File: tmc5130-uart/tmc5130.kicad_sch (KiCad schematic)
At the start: 30 parts, among them J401 Molex_Pico-SPOX_Horizontal, J402 Molex_Pico-Clasp_Horizontal, U401 TMC5160A-WA, U402 MAX6816, X401 16MHz

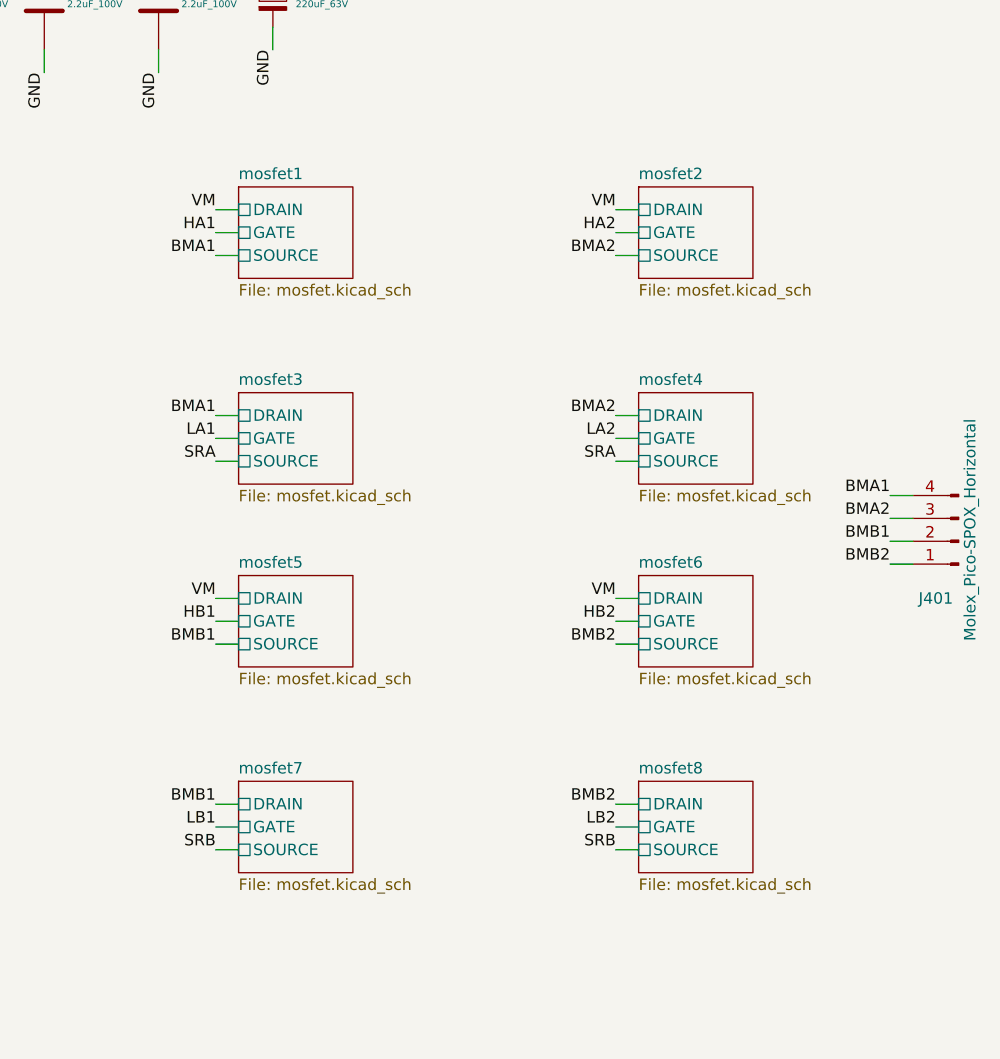
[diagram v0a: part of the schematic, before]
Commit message: Delete unused schematics
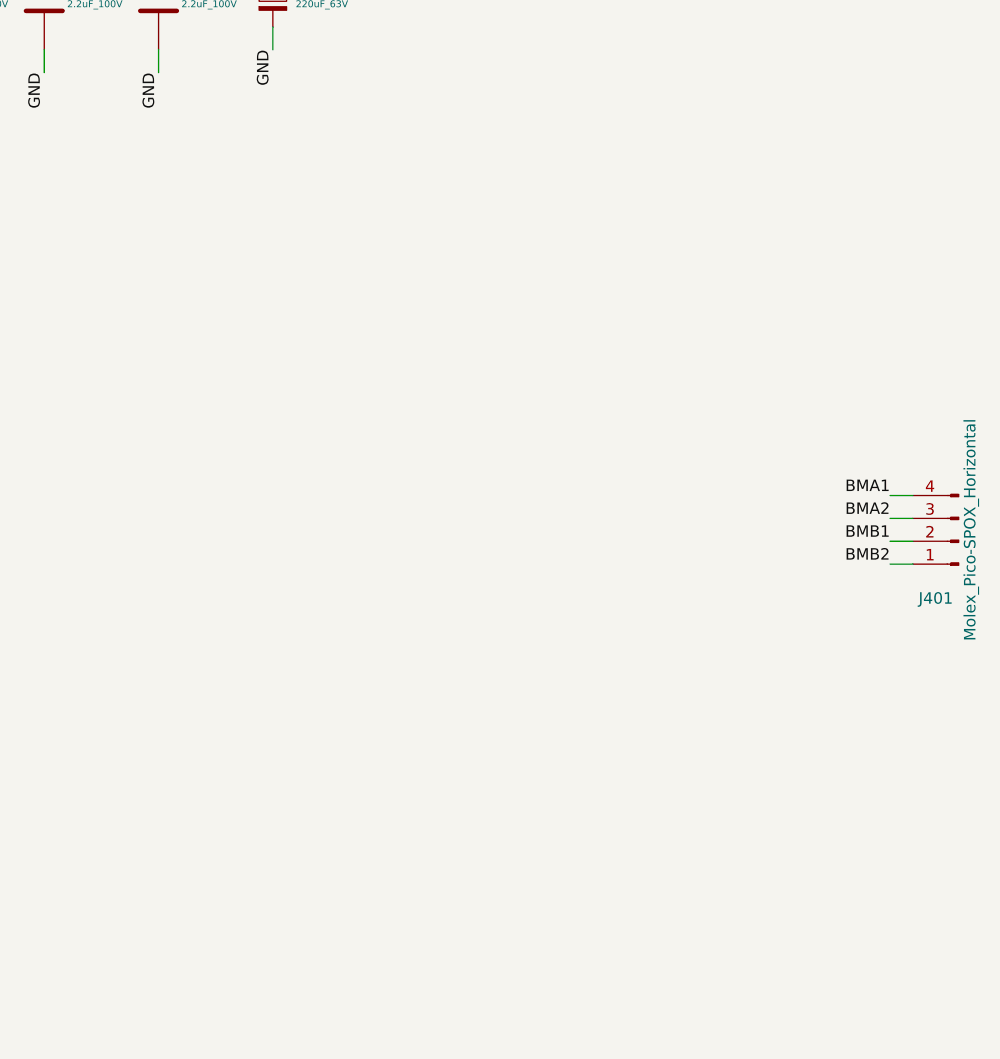
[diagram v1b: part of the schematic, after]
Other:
- removed sheet mosfet1
- removed sheet mosfet2
- removed sheet mosfet3
- removed sheet mosfet4
- removed sheet mosfet5
- removed sheet mosfet6
- removed sheet mosfet7
- removed sheet mosfet8

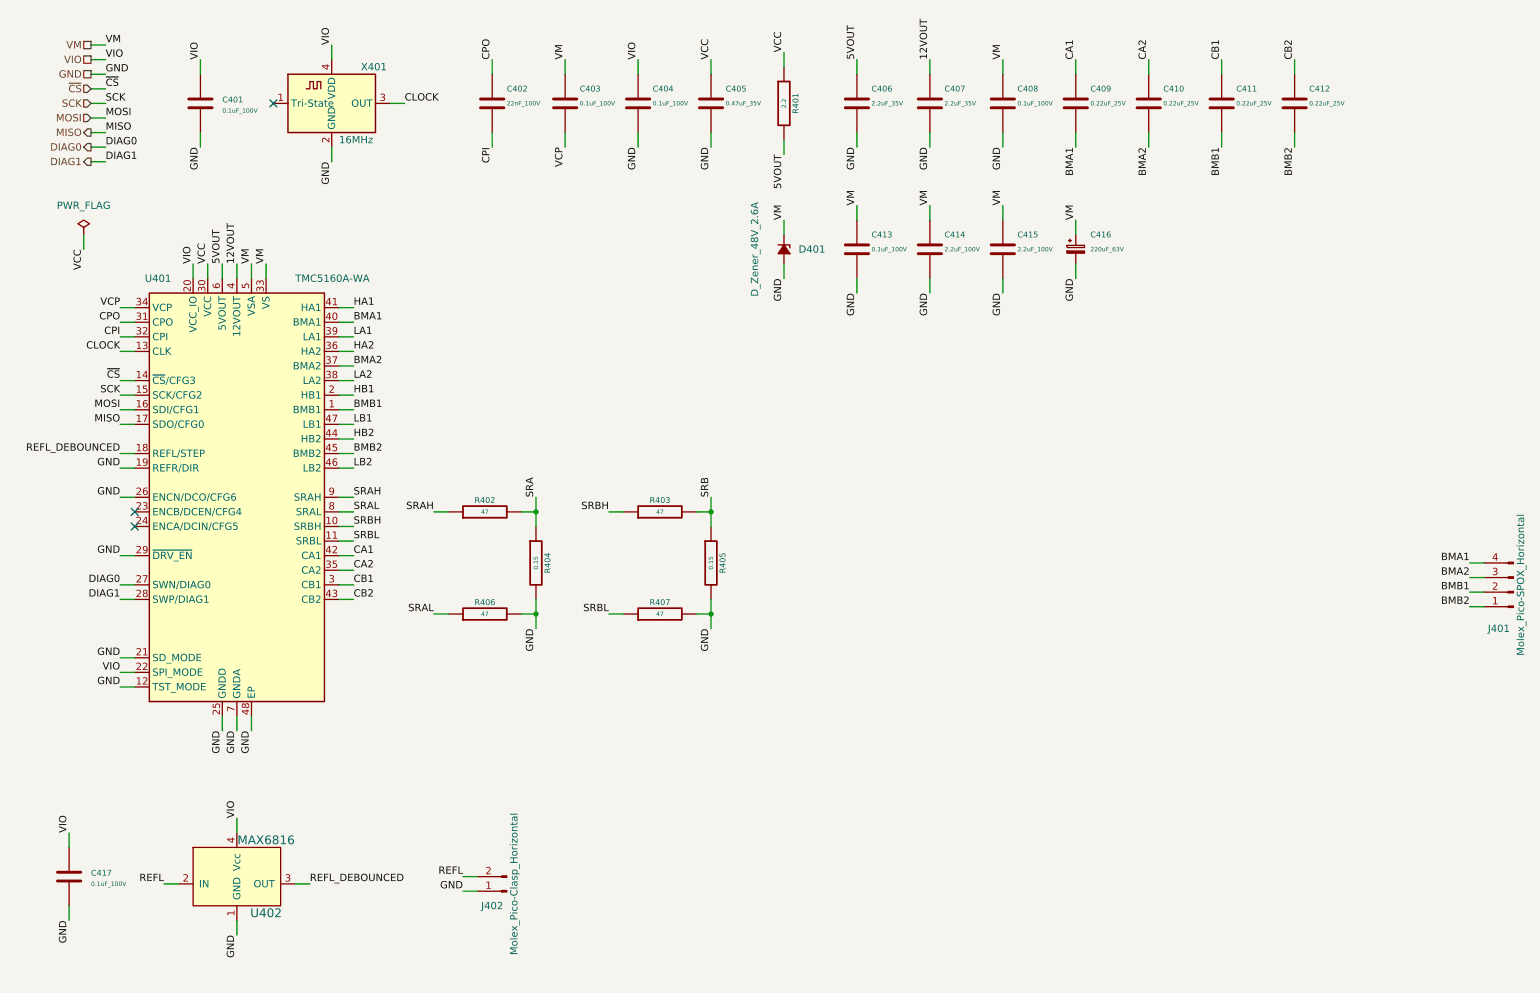
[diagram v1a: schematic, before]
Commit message: TMC5160 -> TMC5130 component
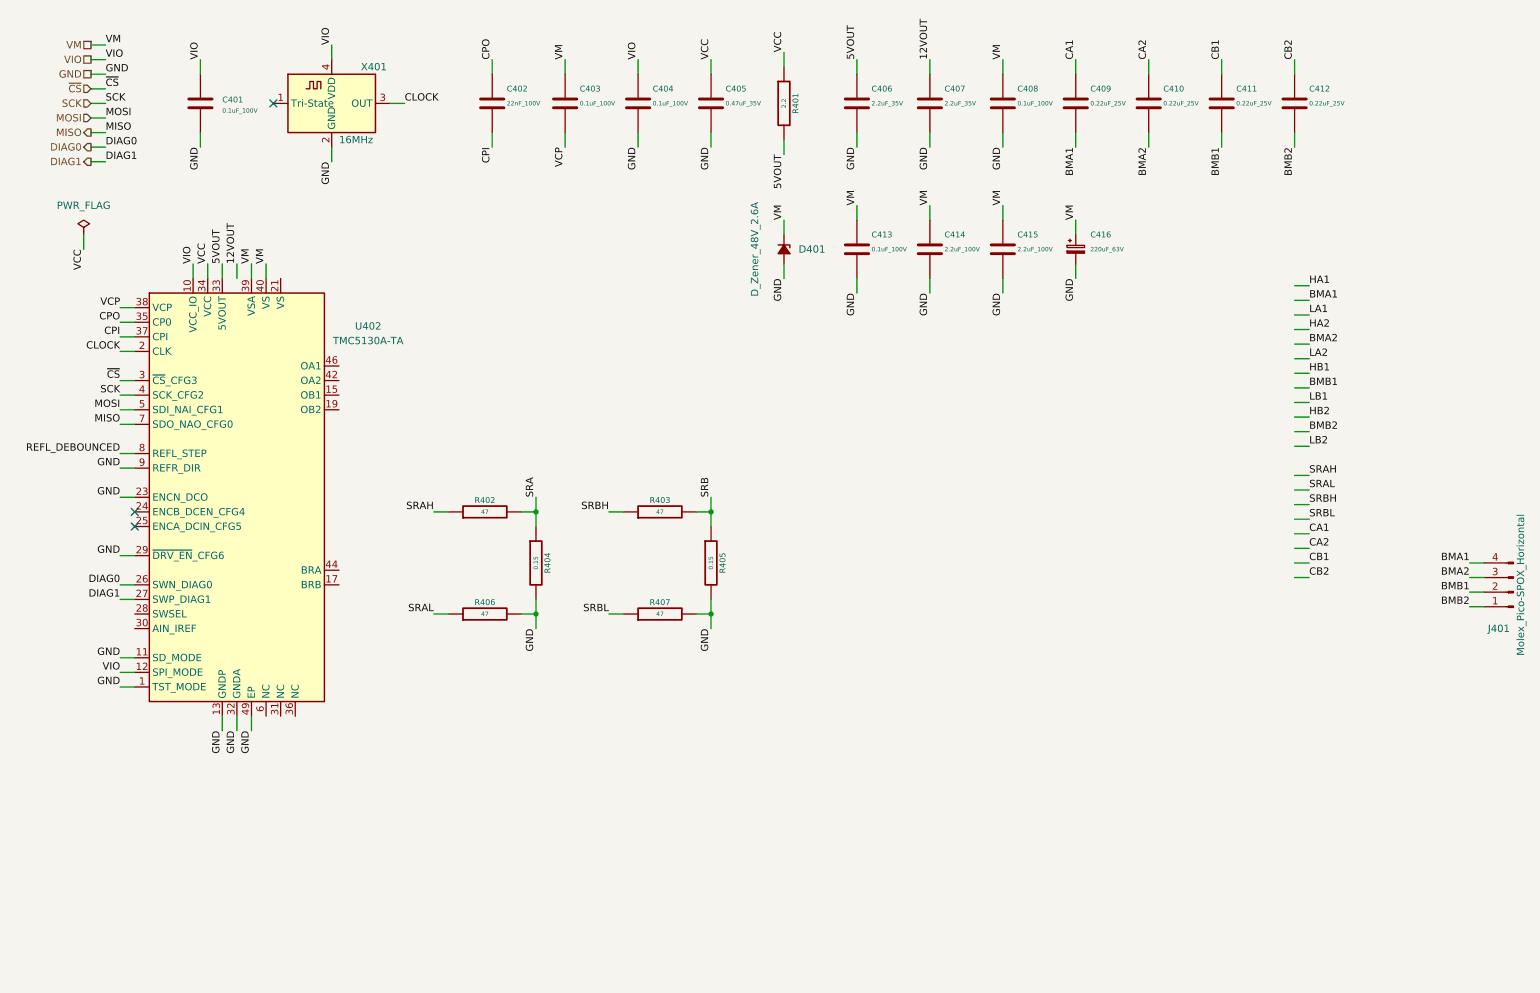
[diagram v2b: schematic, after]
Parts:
- removed C417: 0.1uF_100V, Janelia:C_0402_1005Metric, symbol Janelia:C_0.1uF_100V_0402
- removed J402: Molex_Pico-Clasp_Horizontal, Janelia:Molex_Pico-Clasp-501568_1x02_P1mm_Horizontal, symbol Janelia:Conn_01x02_P1mm_Molex_Pico-Clasp-501330_Horizontal
- removed U401: TMC5160A-WA, Janelia:21-100593_ADI, symbol Janelia:TMC5160A-WA
- removed U402: MAX6816, Janelia:SOT192P237X122-4N, symbol Janelia:MAX6816
- added U402: TMC5130A-TA, Janelia:TQFP-48-1EP_7x7mm_P0.5mm_EP5x5mm_ThermalVias, symbol Janelia:TMC5130A-TA
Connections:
- net 5VOUT: now also U402.33 (5VOUT)
- net CLOCK: now also U402.2 (CLK)
- net CPI: now also U402.37 (CPI)
- net CPO: now also U402.35 (CP0)
- net DIAG0: now also U402.26 (SWN_DIAG0)
- net DIAG1: now also U402.27 (SWP_DIAG1)
- net GND: now also U402.1 (TST_MODE), U402.11 (SD_MODE), U402.13 (GNDP), U402.23 (ENCN_DCO), U402.29 (~{DRV_EN}_CFG6), U402.32 (GNDA), U402.48 (GNDP), U402.49 (EP), U402.9 (REFR_DIR)
- net MISO: now also U402.7 (SDO_NAO_CFG0)
- net MOSI: now also U402.5 (SDI_NAI_CFG1)
- net REFL_DEBOUNCED: now also U402.8 (REFL_STEP)
- net SCK: now also U402.4 (SCK_CFG2)
- net VCC: now also U402.34 (VCC)
- net VCP: now also U402.38 (VCP)
- net VIO: now also U402.10 (VCC_IO), U402.12 (SPI_MODE)
- net VM: now also U402.39 (VSA), U402.40 (VS)
- net ~{CS}: now also U402.3 (~{CS}_CFG3)

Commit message: Add components from jlcpcb
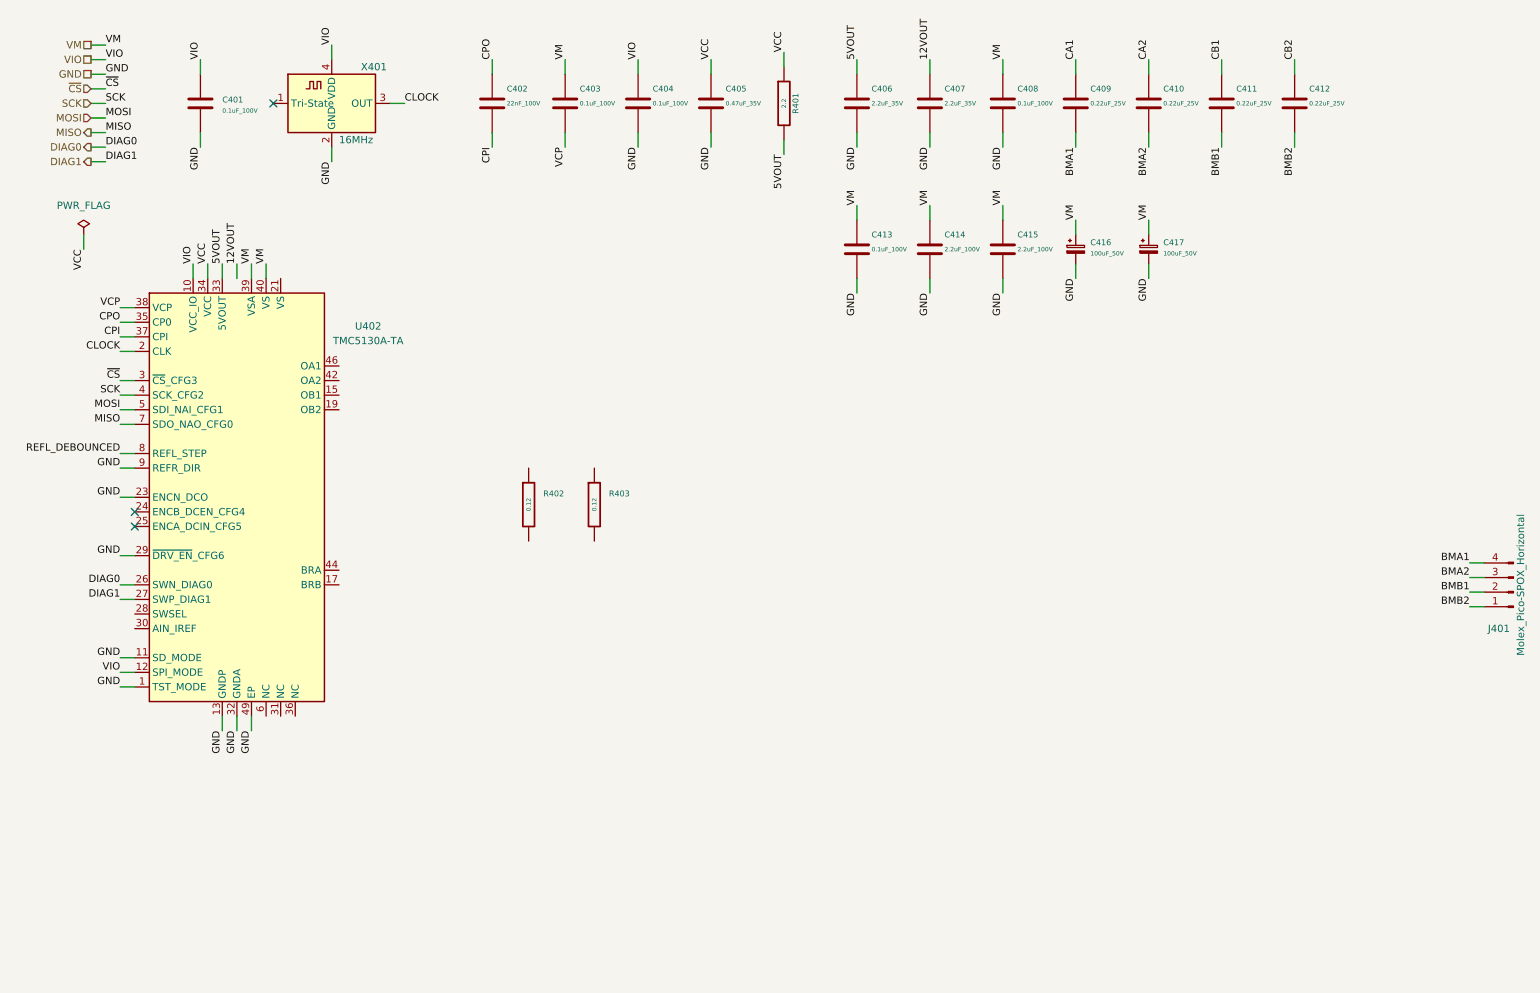
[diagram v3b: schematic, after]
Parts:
- removed C416: 220uF_63V, Janelia:CP_Hybrid_EEHZS1H221V, symbol Janelia:CP_220uF_50V_10.3x10.3mm_Hybrid_Antivib
- removed D401: D_Zener_48V_2.6A, Janelia:SMFSeries_LTF, symbol Janelia:D_Zener_48V_2.6A
- removed R402, R403, R406, R407: 47, Janelia:R_0402_1005Metric, symbol Janelia:R_47_0.063W_0402
- removed R404, R405: 0.15, Janelia:R_1206_3216Metric, symbol Janelia:R_0.15_1W_1206_CS
- added C416, C417: 100uF_50V, Janelia:CAP_EEEFTH101XAV, symbol Janelia:CP_100uF_50V_6.3x8.3mm_Hybrid_Antivib
- added R402, R403: 0.12, Janelia:R_1206_3216Metric, symbol Janelia:R_0.12_750mW_1206_CS
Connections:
- net GND: now also C416.2, C417.2
- net VM: now also C416.1, C417.1
